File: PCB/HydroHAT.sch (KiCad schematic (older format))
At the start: 16 parts, among them IC1 ATMEGA1284P-P, P1 CONN_20X2, P2 CONN_3, P3 CONN_3, P4 CONN_10X2, P5 CONN_8, P6 CONN_4, SW1 SW_PUSH, U1 SN74LVC1T45, U2 SN74LVC1T45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

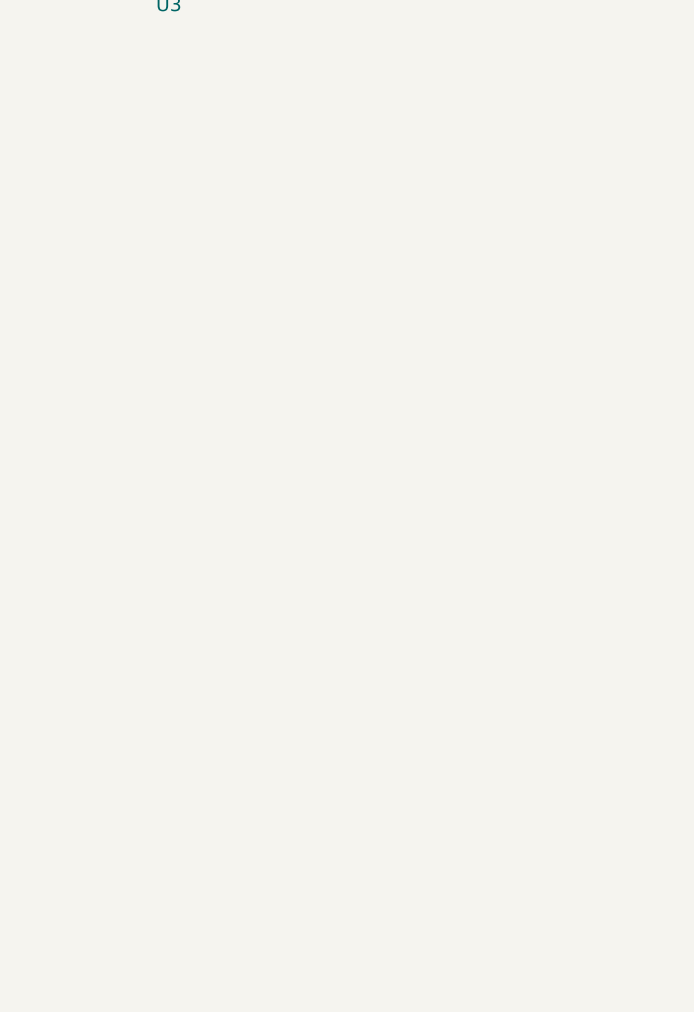
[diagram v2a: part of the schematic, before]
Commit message: Started USB circuitry
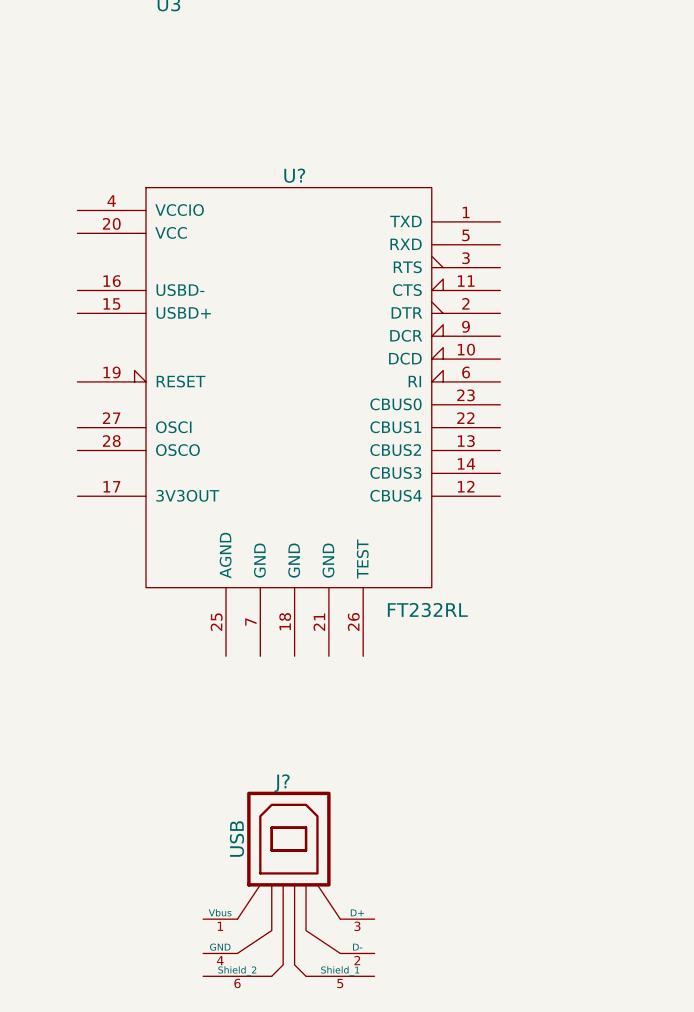
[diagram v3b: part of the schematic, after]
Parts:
- added J?: USB, symbol USB
- added U?: FT232RL, symbol FT232RL
- U1, U2, U3: Distrib Link (none) -> http://www.digikey.com/short/7t7fvf; Distrib PN (none) -> 296-16843-1-ND; MFG Name (none) -> Texas Instruments; MFG Part Num (none) -> SN74LVC1T45DBVR
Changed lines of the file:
@@
 Text GLabel 8950 5400 0    60   Input ~ 0
 IDSD
-Connection ~ 4200 2050
-Wire Wire Line
-	3800 1850 3800 2050
-Wire Wire Line
-	3800 2050 4350 2050
-Wire Wire Line
-	4200 2050 4200 1950
-Wire Wire Line
-	4200 2450 4350 2450
-Wire Wire Line
-	4350 2850 4200 2850
-Wire Wire Line
-	6350 2950 7450 2950
-Wire Wire Line
-	7450 2950 7450 2750
-Wire Wire Line
-	7450 2750 7250 2750
-Wire Wire Line
-	6350 3050 7500 3050
-Wire Wire Line
-	7500 3050 7500 2650
-Wire Wire Line
-	7500 2650 7250 2650
-Wire Wire Line
-	6350 3150 7550 3150
-Wire Wire Line
-	7550 3150 7550 2550
-Wire Wire Line
-	7550 2550 7250 2550
-Wire Wire Line
-	6350 3250 7600 3250
-Wire Wire Line
-	7600 3250 7600 2450
-Wire Wire Line
-	7600 2450 7250 2450
-Wire Wire Line
-	6350 4250 7650 4250
-Wire Wire Line
-	7650 4250 7650 2350
-Wire Wire Line
-	7650 2350 7250 2350
-Wire Wire Line
-	6350 4350 7700 4350
-Wire Wire Line
-	7700 4350 7700 2250
-Wire Wire Line
-	7700 2250 7250 2250
-Wire Wire Line
-	6350 4450 7750 4450
-Wire Wire Line
-	7750 4450 7750 2150
-Wire Wire Line
-	7750 2150 7250 2150
-Wire Wire Line
-	6350 4550 7800 4550
-Wire Wire Line
-	7800 4550 7800 2050
-Wire Wire Line
-	7800 2050 7250 2050
-Wire Wire Line
-	6350 4950 6900 4950
-Wire Wire Line
-	6900 5050 6350 5050
-Wire Wire Line
-	6350 3950 6900 3950
-Wire Wire Line
-	5150 1550 5150 1750
-Wire Wire Line
-	9750 4600 10050 4600
-Wire Wire Line
-	9750 4800 9800 4800
-Wire Wire Line
-	9800 4800 9800 4700
-Wire Wire Line
-	9800 4700 10050 4700
-Wire Wire Line
-	9750 4900 9850 4900
-Wire Wire Line
-	9850 4900 9850 4800
-Wire Wire Line
-	9850 4800 10050 4800
-Wire Wire Line
-	9750 5100 9900 5100
-Wire Wire Line
-	9900 5100 9900 4900
-Wire Wire Line
-	9900 4900 10050 4900
-Wire Wire Line
-	9750 5200 9950 5200
-Wire Wire Line
-	9950 5000 10050 5000
-Wire Wire Line
-	9750 5300 10000 5300
 Text Notes 10100 4400 0    60   ~ 0
 RPi GPIO
@@
 NoConn ~ 9750 4700
 NoConn ~ 9750 5000
-Wire Wire Line
-	8300 4300 8950 4300
-Wire Wire Line
-	9950 5200 9950 5000
-Wire Wire Line
-	10000 5300 10000 5100
-Wire Wire Line
-	10000 5100 10050 5100
-Wire Wire Line
-	9750 5500 10050 5500
-Wire Wire Line
-	10050 5500 10050 5200
 $Comp
 L CONN_8 P5
@@
 	1    0    0    -1
 $EndComp
-Wire Wire Line
-	10050 4500 10050 4200
-Wire Wire Line
-	9750 4200 10150 4200
-Connection ~ 10050 4200
-Wire Wire Line
-	6350 2750 6450 2750
-Wire Wire Line
-	6450 2650 6350 2650
-Wire Wire Line
-	6350 2550 6450 2550
-Wire Wire Line
-	6450 2450 6350 2450
-Wire Wire Line
-	6350 2350 6450 2350
-Wire Wire Line
-	6450 2250 6350 2250
-Wire Wire Line
-	6350 2150 6450 2150
-Wire Wire Line
-	6450 2050 6350 2050
 $Comp
 L CONN_10X2 P4
@@
 Text GLabel 7250 2850 2    60   Input ~ 0
 GND
-Wire Notes Line
-	9200 6200 9500 6200
-Wire Notes Line
-	9500 6200 9500 6300
-Wire Notes Line
-	9500 6300 9200 6300
-Wire Notes Line
-	9200 6300 9200 6200
-Wire Notes Line
-	6750 1650 6750 1750
-Wire Notes Line
-	6750 1750 6950 1750
-Wire Notes Line
-	6950 1750 6950 1650
-Wire Notes Line
-	6950 1650 6750 1650
 $Comp
 L CONN_3 P2
@@
 	-1   0    0    1
 $EndComp
-Wire Wire Line
-	8950 4200 8600 4200
-Wire Wire Line
-	8600 4200 8600 4100
-Wire Wire Line
-	8600 4100 8300 4100
 Text GLabel 8300 4200 2    60   Input ~ 0
 GND
 Text GLabel 6900 3850 0    60   Input ~ 0
 GND
-Wire Wire Line
-	6350 3850 6600 3850
-Wire Wire Line
-	6600 3850 6600 3750
-Wire Wire Line
-	6600 3750 6900 3750
 Text GLabel 8950 4900 0    60   Input ~ 0
 Vdd
-Wire Wire Line
-	5150 1750 5350 1750
 NoConn ~ 4350 3250
 $Comp
@@
 F 1 "SN74LVC1T45" H 1800 2350 60  0000 C CNN
 F 2 "" H 1800 2150 60  0000 C CNN
-F 3 "" H 1800 2150 60  0000 C CNN
+F 3 "http://www.ti.com/lit/ds/symlink/sn74lvc1t45.pdf" H 1800 2150 60  0001 C CNN
+F 4 "Texas Instruments" H 1800 2150 60  0001 C CNN "MFG Name"
+F 5 "SN74LVC1T45DBVR" H 1800 2150 60  0001 C CNN "MFG Part Num"
+F 6 "296-16843-1-ND" H 1800 2150 60  0001 C CNN "Distrib PN"
+F 7 "http://www.digikey.com/short/7t7fvf" H 1800 2150 60  0001 C CNN "Distrib Link"
 	1    1800 2150
-	1    0    0    -1
-$EndComp
-$Comp
-L SN74LVC1T45 U2
-U 1 1 542198A3
-P 1800 2700
-F 0 "U2" H 1800 2500 60  0000 C CNN
-F 1 "SN74LVC1T45" H 1800 2900 60  0000 C CNN
-F 2 "" H 1800 2700 60  0000 C CNN
-F 3 "" H 1800 2700 60  0000 C CNN
-	1    1800 2700
-	1    0    0    -1
-$EndComp
-$Comp
-L SN74LVC1T45 U3
-U 1 1 542198A9
-P 1800 3250
-F 0 "U3" H 1800 3050 60  0000 C CNN
-F 1 "SN74LVC1T45" H 1800 3450 60  0000 C CNN
-F 2 "" H 1800 3250 60  0000 C CNN
-F 3 "" H 1800 3250 60  0000 C CNN
-	1    1800 3250
 	1    0    0    -1
 $EndComp
@@
 Text GLabel 2100 3350 2    60   Input ~ 0
 Vdd
+$Comp
+L SN74LVC1T45 U2
+U 1 1 5421B642
+P 1800 2700
+F 0 "U2" H 1800 2500 60  0000 C CNN
+F 1 "SN74LVC1T45" H 1800 2900 60  0000 C CNN
+F 2 "" H 1800 2700 60  0000 C CNN
+F 3 "http://www.ti.com/lit/ds/symlink/sn74lvc1t45.pdf" H 1800 2700 60  0001 C CNN
+F 4 "Texas Instruments" H 1800 2700 60  0001 C CNN "MFG Name"
+F 5 "SN74LVC1T45DBVR" H 1800 2700 60  0001 C CNN "MFG Part Num"
+F 6 "296-16843-1-ND" H 1800 2700 60  0001 C CNN "Distrib PN"
+F 7 "http://www.digikey.com/short/7t7fvf" H 1800 2700 60  0001 C CNN "Distrib Link"
+	1    1800 2700
+	1    0    0    -1
+$EndComp
+$Comp
+L SN74LVC1T45 U3
+U 1 1 5421B64C
+P 1800 3250
+F 0 "U3" H 1800 3050 60  0000 C CNN
+F 1 "SN74LVC1T45" H 1800 3450 60  0000 C CNN
+F 2 "" H 1800 3250 60  0000 C CNN
+F 3 "http://www.ti.com/lit/ds/symlink/sn74lvc1t45.pdf" H 1800 3250 60  0001 C CNN
+F 4 "Texas Instruments" H 1800 3250 60  0001 C CNN "MFG Name"
+F 5 "SN74LVC1T45DBVR" H 1800 3250 60  0001 C CNN "MFG Part Num"
+F 6 "296-16843-1-ND" H 1800 3250 60  0001 C CNN "Distrib PN"
+F 7 "http://www.digikey.com/short/7t7fvf" H 1800 3250 60  0001 C CNN "Distrib Link"
+	1    1800 3250
+	1    0    0    -1
+$EndComp
+Connection ~ 4200 2050
+Wire Wire Line
+	3800 1850 3800 2050
+Wire Wire Line
+	3800 2050 4350 2050
+Wire Wire Line
+	4200 2050 4200 1950
+Wire Wire Line
+	4200 2450 4350 2450
+Wire Wire Line
+	4350 2850 4200 2850
+Wire Wire Line
+	6350 2950 7450 2950
+Wire Wire Line
+	7450 2950 7450 2750
+Wire Wire Line
+	7450 2750 7250 2750
+Wire Wire Line
+	6350 3050 7500 3050
+Wire Wire Line
+	7500 3050 7500 2650
+Wire Wire Line
+	7500 2650 7250 2650
+Wire Wire Line
+	6350 3150 7550 3150
+Wire Wire Line
+	7550 3150 7550 2550
+Wire Wire Line
+	7550 2550 7250 2550
+Wire Wire Line
+	6350 3250 7600 3250
+Wire Wire Line
+	7600 3250 7600 2450
+Wire Wire Line
+	7600 2450 7250 2450
+Wire Wire Line
+	6350 4250 7650 4250
+Wire Wire Line
+	7650 4250 7650 2350
+Wire Wire Line
+	7650 2350 7250 2350
+Wire Wire Line
+	6350 4350 7700 4350
+Wire Wire Line
+	7700 4350 7700 2250
+Wire Wire Line
+	7700 2250 7250 2250
+Wire Wire Line
+	6350 4450 7750 4450
+Wire Wire Line
+	7750 4450 7750 2150
+Wire Wire Line
+	7750 2150 7250 2150
+Wire Wire Line
+	6350 4550 7800 4550
+Wire Wire Line
+	7800 4550 7800 2050
+Wire Wire Line
+	7800 2050 7250 2050
+Wire Wire Line
+	6350 4950 6900 4950
+Wire Wire Line
+	6900 5050 6350 5050
+Wire Wire Line
+	6350 3950 6900 3950
+Wire Wire Line
+	5150 1550 5150 1750
+Wire Wire Line
+	9750 4600 10050 4600
+Wire Wire Line
+	9750 4800 9800 4800
+Wire Wire Line
+	9800 4800 9800 4700
+Wire Wire Line
+	9800 4700 10050 4700
+Wire Wire Line
+	9750 4900 9850 4900
+Wire Wire Line
+	9850 4900 9850 4800
+Wire Wire Line
+	9850 4800 10050 4800
+Wire Wire Line
+	9750 5100 9900 5100
+Wire Wire Line
+	9900 5100 9900 4900
+Wire Wire Line
+	9900 4900 10050 4900
+Wire Wire Line
+	9750 5200 9950 5200
+Wire Wire Line
+	9950 5000 10050 5000
+Wire Wire Line
+	9750 5300 10000 5300
+Wire Wire Line
+	8300 4300 8950 4300
+Wire Wire Line
+	9950 5200 9950 5000
+Wire Wire Line
+	10000 5300 10000 5100
+Wire Wire Line
+	10000 5100 10050 5100
+Wire Wire Line
+	9750 5500 10050 5500
+Wire Wire Line
+	10050 5500 10050 5200
+Wire Wire Line
+	10050 4500 10050 4200
+Wire Wire Line
+	9750 4200 10150 4200
+Connection ~ 10050 4200
+Wire Wire Line
+	6350 2750 6450 2750
+Wire Wire Line
+	6450 2650 6350 2650
+Wire Wire Line
+	6350 2550 6450 2550
+Wire Wire Line
+	6450 2450 6350 2450
+Wire Wire Line
+	6350 2350 6450 2350
+Wire Wire Line
+	6450 2250 6350 2250
+Wire Wire Line
+	6350 2150 6450 2150
+Wire Wire Line
+	6450 2050 6350 2050
+Wire Notes Line
+	9200 6200 9500 6200
+Wire Notes Line
+	9500 6200 9500 6300
+Wire Notes Line
+	9500 6300 9200 6300
+Wire Notes Line
+	9200 6300 9200 6200
+Wire Notes Line
+	6750 1650 6750 1750
+Wire Notes Line
+	6750 1750 6950 1750
+Wire Notes Line
+	6950 1750 6950 1650
+Wire Notes Line
+	6950 1650 6750 1650
+Wire Wire Line
+	8950 4200 8600 4200
+Wire Wire Line
+	8600 4200 8600 4100
+Wire Wire Line
+	8600 4100 8300 4100
+Wire Wire Line
+	6350 3850 6600 3850
+Wire Wire Line
+	6600 3850 6600 3750
+Wire Wire Line
+	6600 3750 6900 3750
+Wire Wire Line
+	5150 1750 5350 1750
+$Comp
+L FT232RL U?
+U 1 1 5421BA70
+P 2350 5100
+F 0 "U?" H 2350 6000 60  0000 C CNN
+F 1 "FT232RL" H 2750 4100 60  0000 L CNN
+F 2 "" H 2350 5100 60  0000 C CNN
+F 3 "http://www.ftdichip.com/Support/Documents/DataSheets/ICs/DS_FT232R.pdf" H 2350 5100 60  0001 C CNN
+F 4 "FTDI, Future Technology Devices International Ltd" H 2350 5100 60  0001 C CNN "MFG Name"
+F 5 "FT232RL-TUBE" H 2350 5100 60  0001 C CNN "MFG Part Num"
+F 6 "FT232RL-TUBE-ND" H 2350 5100 60  0001 C CNN "Distrib PN"
+F 7 "http://www.digikey.com/short/7t7wj0" H 2350 5100 60  0001 C CNN "Distrib Link"
+	1    2350 5100
+	1    0    0    -1
+$EndComp
+$Comp
+L USB J?
+U 1 1 5421BB71
+P 2350 7250
+F 0 "J?" H 2300 7650 60  0000 C CNN
+F 1 "USB" V 2100 7400 60  0000 C CNN
+F 2 "" H 2350 7250 60  0000 C CNN
+F 3 "" H 2350 7250 60  0000 C CNN
+	1    2350 7250
+	1    0    0    -1
+$EndComp
 $EndSCHEMATC

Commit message: Almost done
Just need to add two datasheets
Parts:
- added C4: 0.1uF, ~, symbol C
- added IC3: CAT24C32, symbol CAT24C32
- added P7: CONN_5, symbol CONN_5
- J1: renamed from J?; value USB -> USB-B; Distrib Link (none) -> http://www.digikey.com/short/7t3f2f; Distrib PN (none) -> 952-1767-ND; MFG Name (none) -> Harwin Inc; MFG Part Num (none) -> M701-330442
- P2, P3: Distrib Link (none) -> http://www.digikey.com/short/7t32b0; Distrib PN (none) -> A19470-ND; MFG Name (none) -> TE Connectivity; MFG Part Num (none) -> 640456-3
- P5: Distrib Link (none) -> http://www.digikey.com/short/7t3278; Distrib PN (none) -> A1924-ND; MFG Name (none) -> TE Connectivity; MFG Part Num (none) -> 640456-8
- P6: Distrib Link (none) -> http://www.digikey.com/short/7t32pm; Distrib PN (none) -> A1922-ND; MFG Name (none) -> TE Connectivity; MFG Part Num (none) -> 640456-4
- gave numbers to parts that had none: 2
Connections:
- net DTR: now also IC2.2 (DTR)
- net GND: now also IC2.18 (GND), IC2.21 (GND), IC2.25 (AGND), IC2.26 (TEST), IC2.7 (GND), J1.4 (GND), C4.1, IC3.4 (GND), P7.2
- net IDSC: now also IC3.6 (SCL)
- net IDSD: now also IC3.5 (SDA)
- net RXD: now also IC2.1 (TXD)
- net SRX: now also P7.4
- net STX: now also P7.3
- net TXD: now also IC2.5 (RXD)
- net Vcc: now also IC2.20 (VCC), IC2.4 (VCCIO), C4.2, P7.5
- net Vdd: now also IC3.8 (Vcc)
- net PEN: now reaches IC1.18 ((PCINT28/XCK1/OC1B)PD4)
- net PEN: now also IC2.14 (CBUS3)
- net at C1.2, C2.1, IC1.9 (~RESET)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: now also SW1.1
- net at IC2.15 (USBD+): now also J1.3 (D+)
- net at IC2.16 (USBD-): now also J1.2 (D-)
- no-connect marks 27 -> 47
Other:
- note added: "4D Systems Connector"
- moved on the sheet: J1
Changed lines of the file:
@@
 Sheet 1 1
 Title "HydroHAT Hydroponics Control Board"
-Date "23 sep 2014"
+Date "24 sep 2014"
 Rev "1"
 Comp "Rancho High School"
@@
 $EndComp
 $Comp
-L RESONATOR_C RES?
+L RESONATOR_C RES1
 U 1 1 5420AE48
 P 4000 2650
-F 0 "RES?" H 4000 3000 60  0000 C CNN
+F 0 "RES1" H 4000 3000 60  0000 C CNN
 F 1 "20MHz" H 4000 2300 60  0000 C CNN
 F 2 "" H 4000 3050 60  0000 C CNN
@@
 NoConn ~ 6350 5350
 NoConn ~ 6350 5250
-NoConn ~ 6350 5150
 $Comp
 L CONN_4 P6
@@
 F 1 "CONN_4" V 7300 5000 50  0000 C CNN
 F 2 "" H 7250 5000 60  0000 C CNN
-F 3 "" H 7250 5000 60  0000 C CNN
+F 3 "http://www.te.com/commerce/DocumentDelivery/DDEController?Action=srchrtrv&DocNm=640456&DocType=Customer+Drawing&DocLang=English" H 7250 5000 60  0001 C CNN
+F 4 "TE Connectivity" H 7250 5000 60  0001 C CNN "MFG Name"
+F 5 "640456-4" H 7250 5000 60  0001 C CNN "MFG Part Num"
+F 6 "A1922-ND" H 7250 5000 60  0001 C CNN "Distrib PN"
+F 7 "http://www.digikey.com/short/7t32pm" H 7250 5000 60  0001 C CNN "Distrib Link"
 	1    7250 5000
 	1    0    0    -1
@@
 F 1 "CONN_8" V 10450 4850 60  0000 C CNN
 F 2 "" H 10400 4850 60  0000 C CNN
-F 3 "" H 10400 4850 60  0000 C CNN
+F 3 "http://www.te.com/commerce/DocumentDelivery/DDEController?Action=srchrtrv&DocNm=640456&DocType=Customer+Drawing&DocLang=English" H 10400 4850 60  0001 C CNN
+F 4 "TE Connectivity" H 10400 4850 60  0001 C CNN "MFG Name"
+F 5 "640456-8" H 10400 4850 60  0001 C CNN "MFG Part Num"
+F 6 "A1924-ND" H 10400 4850 60  0001 C CNN "Distrib PN"
+F 7 "http://www.digikey.com/short/7t3278" H 10400 4850 60  0001 C CNN "Distrib Link"
 	1    10400 4850
 	1    0    0    -1
@@
 F 1 "CONN_3" V 7300 3850 40  0000 C CNN
 F 2 "" H 7250 3850 60  0000 C CNN
-F 3 "" H 7250 3850 60  0000 C CNN
+F 3 "http://www.te.com/commerce/DocumentDelivery/DDEController?Action=srchrtrv&DocNm=640456&DocType=Customer+Drawing&DocLang=English" H 7250 3850 60  0001 C CNN
+F 4 "TE Connectivity" H 7250 3850 60  0001 C CNN "MFG Name"
+F 5 "640456-3" H 7250 3850 60  0001 C CNN "MFG Part Num"
+F 6 "A19470-ND" H 7250 3850 60  0001 C CNN "Distrib PN"
+F 7 "http://www.digikey.com/short/7t32b0" H 7250 3850 60  0001 C CNN "Distrib Link"
 	1    7250 3850
 	1    0    0    -1
-$EndComp
-$Comp
-L CONN_3 P3
-U 1 1 5420F13B
-P 7950 4200
-F 0 "P3" V 7900 4200 50  0000 C CNN
-F 1 "CONN_3" V 8000 4200 40  0000 C CNN
-F 2 "" H 7950 4200 60  0000 C CNN
-F 3 "" H 7950 4200 60  0000 C CNN
-	1    7950 4200
-	-1   0    0    1
 $EndComp
 Text GLabel 8300 4200 2    60   Input ~ 0
@@
 	1    0    0    -1
 $EndComp
+$Comp
+L FT232RL IC2
+U 1 1 5421BA70
+P 2350 5100
+F 0 "IC2" H 2350 6000 60  0000 C CNN
+F 1 "FT232RL" H 2750 4100 60  0000 L CNN
+F 2 "" H 2350 5100 60  0000 C CNN
+F 3 "http://www.ftdichip.com/Support/Documents/DataSheets/ICs/DS_FT232R.pdf" H 2350 5100 60  0001 C CNN
+F 4 "FTDI, Future Technology Devices International Ltd" H 2350 5100 60  0001 C CNN "MFG Name"
+F 5 "FT232RL-TUBE" H 2350 5100 60  0001 C CNN "MFG Part Num"
+F 6 "FT232RL-TUBE-ND" H 2350 5100 60  0001 C CNN "Distrib PN"
+F 7 "http://www.digikey.com/short/7t7wj0" H 2350 5100 60  0001 C CNN "Distrib Link"
+	1    2350 5100
+	1    0    0    -1
+$EndComp
+$Comp
+L USB J1
+U 1 1 5421BB71
+P 1050 5050
+F 0 "J1" H 1000 5450 60  0000 C CNN
+F 1 "USB-B" V 800 5200 60  0000 C CNN
+F 2 "" H 1050 5050 60  0000 C CNN
+F 3 "http://harwin.com/includes/pdfs/M701-330442.pdf" H 1050 5050 60  0001 C CNN
+F 4 "Harwin Inc" H 1050 5050 60  0001 C CNN "MFG Name"
+F 5 "M701-330442" H 1050 5050 60  0001 C CNN "MFG Part Num"
+F 6 "952-1767-ND" H 1050 5050 60  0001 C CNN "Distrib PN"
+F 7 "http://www.digikey.com/short/7t3f2f" H 1050 5050 60  0001 C CNN "Distrib Link"
+	1    1050 5050
+	1    0    0    1
+$EndComp
 Connection ~ 4200 2050
 Wire Wire Line
@@
 Wire Wire Line
 	5150 1750 5350 1750
-$Comp
-L FT232RL U?
-U 1 1 5421BA70
-P 2350 5100
-F 0 "U?" H 2350 6000 60  0000 C CNN
-F 1 "FT232RL" H 2750 4100 60  0000 L CNN
-F 2 "" H 2350 5100 60  0000 C CNN
-F 3 "http://www.ftdichip.com/Support/Documents/DataSheets/ICs/DS_FT232R.pdf" H 2350 5100 60  0001 C CNN
-F 4 "FTDI, Future Technology Devices International Ltd" H 2350 5100 60  0001 C CNN "MFG Name"
-F 5 "FT232RL-TUBE" H 2350 5100 60  0001 C CNN "MFG Part Num"
-F 6 "FT232RL-TUBE-ND" H 2350 5100 60  0001 C CNN "Distrib PN"
-F 7 "http://www.digikey.com/short/7t7wj0" H 2350 5100 60  0001 C CNN "Distrib Link"
-	1    2350 5100
-	1    0    0    -1
-$EndComp
-$Comp
-L USB J?
-U 1 1 5421BB71
-P 2350 7250
-F 0 "J?" H 2300 7650 60  0000 C CNN
-F 1 "USB" V 2100 7400 60  0000 C CNN
-F 2 "" H 2350 7250 60  0000 C CNN
-F 3 "" H 2350 7250 60  0000 C CNN
-	1    2350 7250
-	1    0    0    -1
-$EndComp
+Wire Wire Line
+	1400 4850 1400 4800
+Text GLabel 550  4600 1    60   Input ~ 0
+GND
+Wire Wire Line
+	550  4600 550  4700
+Wire Wire Line
+	550  4700 650  4700
+NoConn ~ 650  4850
+NoConn ~ 650  4600
+NoConn ~ 1400 4600
+Text GLabel 1400 4250 1    60   Input ~ 0
+Vcc
+Wire Wire Line
+	2050 6300 2050 6400
+Wire Wire Line
+	2050 6400 2650 6400
+Wire Wire Line
+	2650 6400 2650 6300
+Wire Wire Line
+	2500 6300 2500 6400
+Wire Wire Line
+	2500 6400 2200 6400
+Connection ~ 2200 6400
+Wire Wire Line
+	2200 6400 2200 6300
+Connection ~ 2500 6400
+Wire Wire Line
+	2350 6300 2350 6500
+Connection ~ 2350 6400
+Text GLabel 2350 6500 3    60   Input ~ 0
+GND
+Text GLabel 3250 4800 2    60   Input ~ 0
+DTR
+Text GLabel 3250 4400 2    60   Input ~ 0
+RXD
+Text GLabel 3250 4500 2    60   Input ~ 0
+TXD
+Text GLabel 6350 5150 2    60   Input ~ 0
+PEN
+Text GLabel 3250 5500 2    60   Input ~ 0
+PEN
+$Comp
+L C C4
+U 1 1 5422E16F
+P 1200 4350
+F 0 "C4" H 1200 4450 40  0000 L CNN
+F 1 "0.1uF" H 1206 4265 40  0000 L CNN
+F 2 "~" H 1238 4200 30  0000 C CNN
+F 3 "http://www.avx.com/docs/Catalogs/skycap-sr.pdf" H 1200 4350 60  0001 C CNN
+F 4 "AVX Corporation" H 1200 4350 60  0001 C CNN "MFG Name"
+F 5 "SR295E104MAR" H 1200 4350 60  0001 C CNN "MFG Part Num"
+F 6 "478-5741-ND" H 1200 4350 60  0001 C CNN "Distrib PN"
+F 7 "http://www.digikey.com/short/77v1wd" H 1200 4350 60  0001 C CNN "Distrib Link"
+	1    1200 4350
+	0    -1   -1   0
+$EndComp
+Text GLabel 1000 4350 1    60   Input ~ 0
+GND
+Wire Wire Line
+	1400 4250 1400 4450
+Connection ~ 4000 2050
+Connection ~ 3800 2050
+Connection ~ 1400 4350
+Connection ~ 1400 4450
+NoConn ~ 1400 5100
+NoConn ~ 1400 5300
+NoConn ~ 1400 5400
+NoConn ~ 1400 5600
+NoConn ~ 3250 5600
+NoConn ~ 3250 5400
+NoConn ~ 3250 5300
+NoConn ~ 3250 5200
+NoConn ~ 3250 5100
+NoConn ~ 3250 5000
+NoConn ~ 3250 4900
+NoConn ~ 3250 4700
+NoConn ~ 3250 4600
+Connection ~ 5150 1750
+Connection ~ 5350 1750
+Connection ~ 5150 1550
+Connection ~ 1000 4350
+$Comp
+L CONN_3 P3
+U 1 1 5422E631
+P 7950 4200
+F 0 "P3" V 7900 4200 50  0000 C CNN
+F 1 "CONN_3" V 8000 4200 40  0000 C CNN
+F 2 "" H 7950 4200 60  0000 C CNN
+F 3 "http://www.te.com/commerce/DocumentDelivery/DDEController?Action=srchrtrv&DocNm=640456&DocType=Customer+Drawing&DocLang=English" H 7950 4200 60  0001 C CNN
+F 4 "TE Connectivity" H 7950 4200 60  0001 C CNN "MFG Name"
+F 5 "640456-3" H 7950 4200 60  0001 C CNN "MFG Part Num"
+F 6 "A19470-ND" H 7950 4200 60  0001 C CNN "Distrib PN"
+F 7 "http://www.digikey.com/short/7t32b0" H 7950 4200 60  0001 C CNN "Distrib Link"
+	1    7950 4200
+	-1   0    0    1
+$EndComp
+$Comp
+L CAT24C32 IC3
+U 1 1 542310FC
+P 7350 6250
+F 0 "IC3" H 7350 6000 60  0000 C CNN
+F 1 "CAT24C32" H 7350 6500 60  0000 C CNN
+F 2 "" H 7350 6250 60  0000 C CNN
+F 3 "" H 7350 6250 60  0000 C CNN
+	1    7350 6250
+	1    0    0    -1
+$EndComp
+NoConn ~ 7050 6100
+NoConn ~ 7050 6200
+NoConn ~ 7050 6300
+NoConn ~ 7650 6200
+Text GLabel 7650 6100 2    60   Input ~ 0
+Vdd
+Text GLabel 7050 6400 0    60   Input ~ 0
+GND
+Text GLabel 7650 6300 2    60   Input ~ 0
+IDSC
+Text GLabel 7650 6400 2    60   Input ~ 0
+IDSD
+$Comp
+L CONN_5 P7
+U 1 1 542311A8
+P 4450 7350
+F 0 "P7" V 4400 7350 50  0000 C CNN
+F 1 "CONN_5" V 4500 7350 50  0000 C CNN
+F 2 "" H 4450 7350 60  0000 C CNN
+F 3 "" H 4450 7350 60  0000 C CNN
+	1    4450 7350
+	0    1    1    0
+$EndComp
+NoConn ~ 4650 6950
+Text GLabel 4550 6950 1    60   Input ~ 0
+GND
+Text GLabel 4250 6950 1    60   Input ~ 0
+Vcc
+Text GLabel 4450 6950 1    60   Input ~ 0
+STX
+Text GLabel 4350 6950 1    60   Input ~ 0
+SRX
+Text Notes 3900 7550 0    60   ~ 0
+4D Systems Connector
 $EndSCHEMATC
